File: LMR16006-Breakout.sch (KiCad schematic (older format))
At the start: 14 parts, among them P1 CONN_01X04, U1 LMR16006

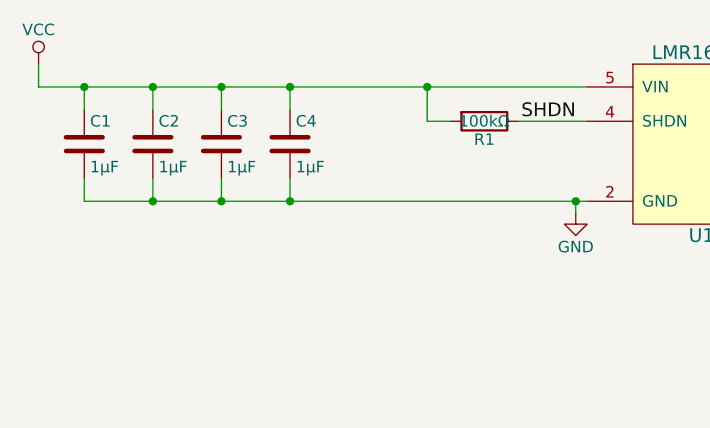
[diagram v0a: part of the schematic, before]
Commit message: update 3d view, some tweaks, silkscreen
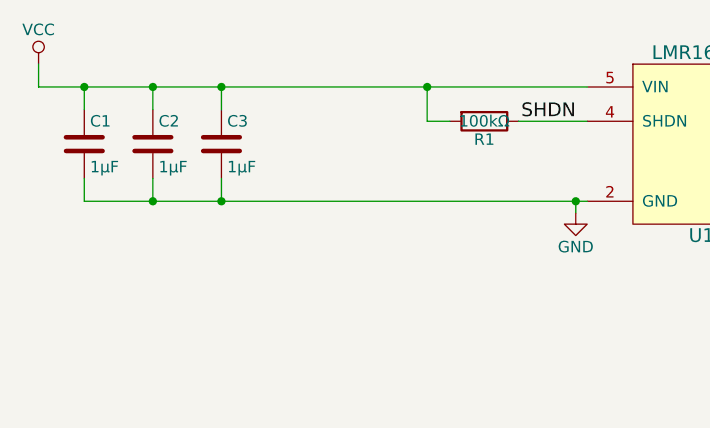
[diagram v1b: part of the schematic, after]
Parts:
- removed C4: 1µF, Capacitors_SMD:C_1206, symbol C
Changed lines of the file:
@@
 	4650 3250 4950 3250
-$Comp
-L C C4
-U 1 1 58E203FB
-P 3650 3350
-F 0 "C4" H 3675 3450 50  0000 L CNN
-F 1 "1µF" H 3675 3250 50  0000 L CNN
-F 2 "Capacitors_SMD:C_1206" H 3688 3200 50  0001 C CNN
-F 3 "" H 3650 3350 50  0000 C CNN
-	1    3650 3350
-	1    0    0    -1
-$EndComp
 $Comp
 L C C3
@@
 Connection ~ 3350 3600
 Wire Wire Line
-	3650 3500 3650 3600
-Connection ~ 3650 3600
-Wire Wire Line
 	2550 3100 4950 3100
 Wire Wire Line
@@
 	3350 3100 3350 3200
 Connection ~ 3350 3100
-Wire Wire Line
-	3650 3100 3650 3200
-Connection ~ 3650 3100
 $Comp
 L VCC #PWR05
